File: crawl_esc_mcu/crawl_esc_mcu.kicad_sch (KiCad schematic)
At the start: 43 parts, among them IC1 LP2981-33DBVTE4, IC2 STM32F051K8U7_MY, IC3 FD6288Q

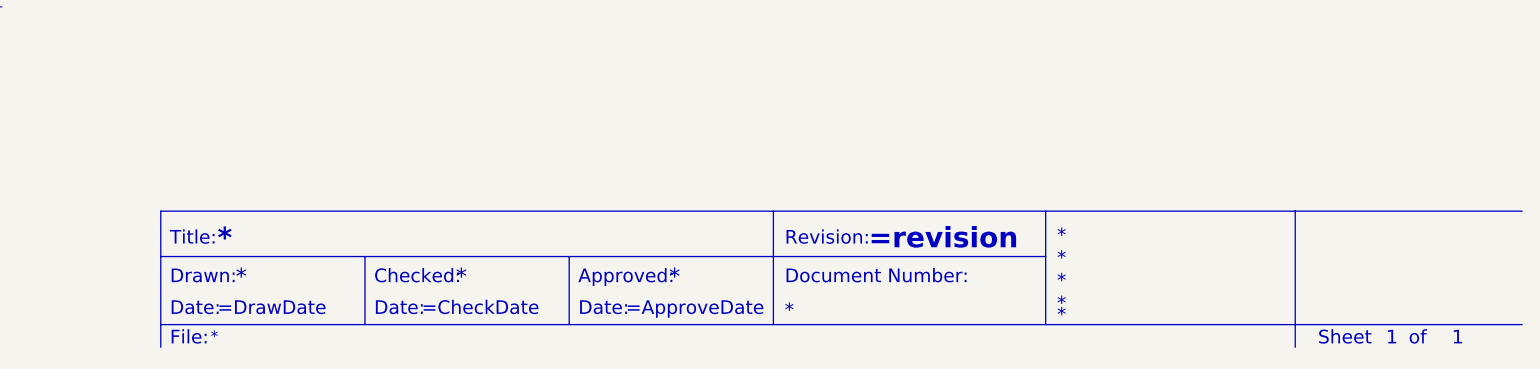
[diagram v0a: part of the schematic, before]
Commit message: change stepup isens layout
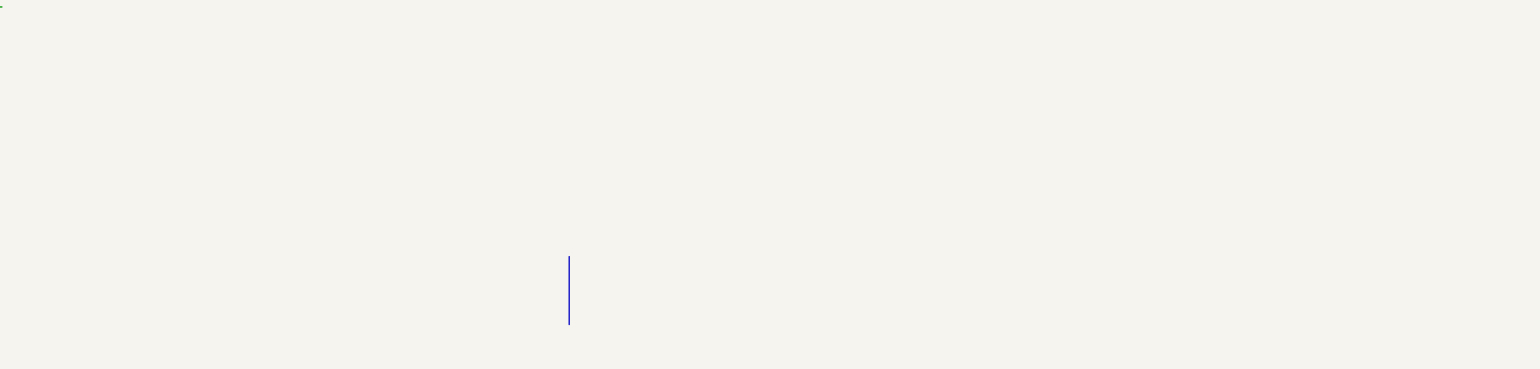
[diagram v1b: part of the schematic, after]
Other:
- note removed: "*"
- note removed: "1"
- note removed: "=ApproveDate"
- note removed: "=CheckDate"
- note removed: "=DrawDate"
- note removed: "=revision"
- note removed: "Approved:"
- note removed: "Checked:"
- note removed: "Date:"
- note removed: "Document Number:"
- note removed: "Drawn:"
- note removed: "File:"
- note removed: "Revision:"
- note removed: "Sheet"
- note removed: "Title:"
- note removed: "of"
